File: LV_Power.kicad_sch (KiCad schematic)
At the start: 0 parts

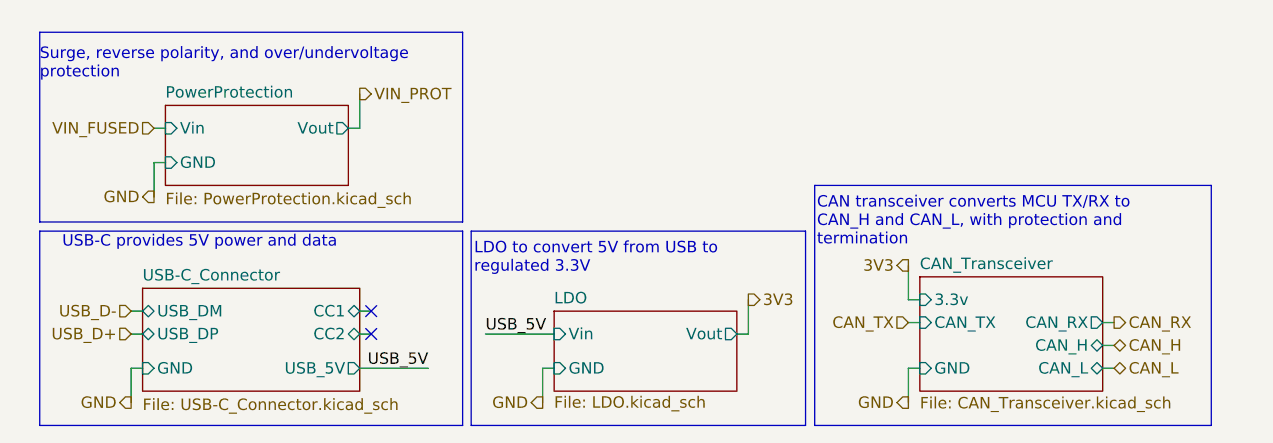
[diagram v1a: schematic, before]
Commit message: seperated hv+ and hv- for main and motor
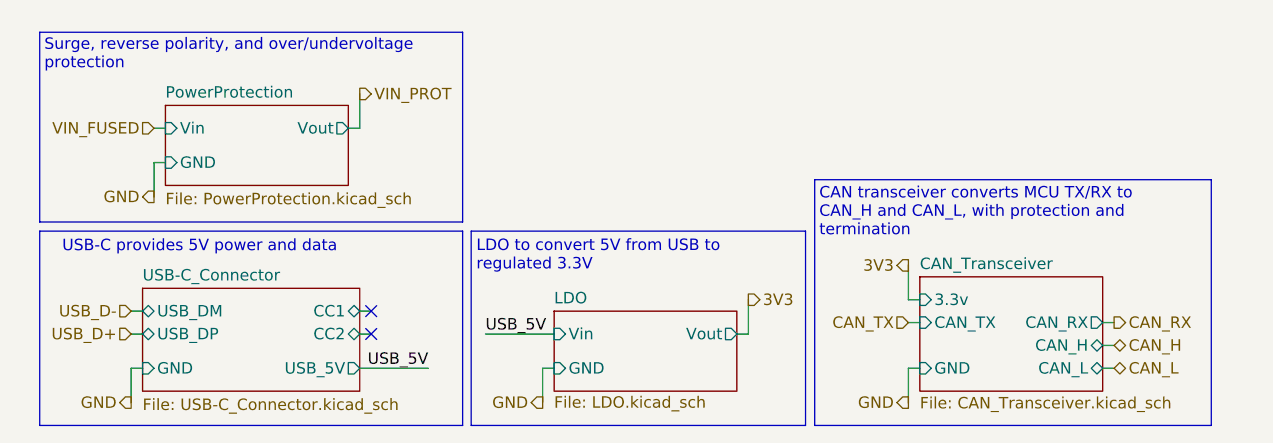
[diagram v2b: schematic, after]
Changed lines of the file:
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@@
 	(paper "A4")
 	(rectangle
-		(start 100.076 31.75)
+		(start 100.076 31.115)
 		(end 144.145 58.42)
 		(stroke
@@
 	(text "LDO to convert 5V from USB to \nregulated 3.3V"
 		(exclude_from_sim no)
-		(at 62.23 38.1 0)
+		(at 62.484 37.846 0)
 		(effects
 			(font
@@
 	(text "Surge, reverse polarity, and over/undervoltage \nprotection"
 		(exclude_from_sim no)
-		(at 13.97 16.51 0)
+		(at 14.478 15.494 0)
 		(effects
 			(font
@@
 	(text "USB-C provides 5V power and data"
 		(exclude_from_sim no)
-		(at 31.75 38.1 0)
+		(at 31.75 38.608 0)
 		(effects
 			(font
@@
 	(text "CAN transceiver converts MCU TX/RX to \nCAN_H and CAN_L, with protection and \ntermination"
 		(exclude_from_sim no)
-		(at 100.33 33.02 0)
+		(at 100.584 32.004 0)
 		(effects
 			(font

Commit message: dnp 0 ohm resistor across power protection
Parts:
- added R?: 0, symbol Device:R
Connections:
- net VIN_FUSED: now also R?.1
- net VIN_PROT: now also R?.2
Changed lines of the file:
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@@
 		)
+	)
+	(junction
+		(at 48.26 25.4)
+		(diameter 0)
+		(color 0 0 0 0)
+	)
+	(junction
+		(at 27.94 25.4)
+		(diameter 0)
+		(color 0 0 0 0)
 	)
 	(no_connect
@@
 	(wire
 		(pts
+			(xy 27.94 26.67) (xy 27.94 25.4)
+		)
+		(stroke
+			(width 0)
+			(type default)
+		)
+	)
+	(wire
+		(pts
 			(xy 110.49 46.99) (xy 111.76 46.99)
 		)
@@
 	(wire
 		(pts
+			(xy 27.94 26.67) (xy 34.29 26.67)
+		)
+		(stroke
+			(width 0)
+			(type default)
+		)
+	)
+	(wire
+		(pts
 			(xy 92.71 48.26) (xy 91.44 48.26)
 		)
@@
 	(wire
 		(pts
+			(xy 41.91 26.67) (xy 48.26 26.67)
+		)
+		(stroke
+			(width 0)
+			(type default)
+		)
+	)
+	(wire
+		(pts
 			(xy 110.49 52.07) (xy 111.76 52.07)
 		)
@@
 		(pts
 			(xy 110.49 44.45) (xy 110.49 40.64)
+		)
+		(stroke
+			(width 0)
+			(type default)
+		)
+	)
+	(wire
+		(pts
+			(xy 48.26 26.67) (xy 48.26 25.4)
 		)
 		(stroke
@@
 		)
 	)
+	(symbol
+		(lib_id "Device:R")
+		(at 38.1 26.67 90)
+		(unit 1)
+		(body_style 1)
+		(exclude_from_sim no)
+		(in_bom yes)
+		(on_board yes)
+		(in_pos_files yes)
+		(dnp yes)
+		(property "Reference" "R?"
+			(at 38.1 24.638 90)
+			(show_name no)
+			(do_not_autoplace no)
+			(effects
+				(font
+					(size 1.27 1.27)
+				)
+			)
+		)
+		(property "Value" "0"
+			(at 38.1 28.956 90)
+			(show_name no)
+			(do_not_autoplace no)
+			(effects
+				(font
+					(size 1.27 1.27)
+				)
+			)
+		)
+		(property "Footprint" ""
+			(at 38.1 28.448 90)
+			(hide yes)
+			(show_name no)
+			(do_not_autoplace no)
+			(effects
+				(font
+					(size 1.27 1.27)
+				)
+			)
+		)
+		(property "Datasheet" ""
+			(at 38.1 26.67 0)
+			(hide yes)
+			(show_name no)
+			(do_not_autoplace no)
+			(effects
+				(font
+					(size 1.27 1.27)
+				)
+			)
+		)
+		(property "Description" "Resistor"
+			(at 38.1 26.67 0)
+			(hide yes)
+			(show_name no)
+			(do_not_autoplace no)
+			(effects
+				(font
+					(size 1.27 1.27)
+				)
+			)
+		)
+		(pin "2"
+		)
+		(pin "1"
+		)
+		(instances
+			(project "PS-PrechargeBoard"
+				(path "/74d17fe6-68d4-4bd7-954a-e2bbb58b1f1e/2ca150cf-fbe5-4d5b-a7dc-f2dc5c6024d0"
+					(reference "R?")
+					(unit 1)
+				)
+			)
+		)
+	)

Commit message: AGND
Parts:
- gave numbers to parts that had none: 1
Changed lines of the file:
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@@
 	(text "LDO to convert 5V from USB to \nregulated 3.3V"
 		(exclude_from_sim no)
-		(at 62.484 37.846 0)
+		(at 62.23 38.1 0)
 		(effects
 			(font
@@
 	(text "Surge, reverse polarity, and over/undervoltage \nprotection"
 		(exclude_from_sim no)
-		(at 14.478 15.494 0)
+		(at 13.97 15.24 0)
 		(effects
 			(font
@@
 	(text "USB-C provides 5V power and data"
 		(exclude_from_sim no)
-		(at 31.75 38.608 0)
+		(at 31.75 38.1 0)
 		(effects
 			(font
@@
 	(text "CAN transceiver converts MCU TX/RX to \nCAN_H and CAN_L, with protection and \ntermination"
 		(exclude_from_sim no)
-		(at 100.584 32.004 0)
+		(at 100.33 31.75 0)
 		(effects
 			(font
@@
 	)
 	(hierarchical_label "GND"
-		(shape output)
+		(shape bidirectional)
 		(at 69.85 55.88 180)
 		(effects
@@
 	)
 	(hierarchical_label "GND"
-		(shape output)
+		(shape bidirectional)
 		(at 24.13 55.88 180)
 		(effects
@@
 	)
 	(hierarchical_label "GND"
-		(shape output)
+		(shape bidirectional)
 		(at 26.67 33.02 180)
 		(effects
@@
 	)
 	(hierarchical_label "GND"
-		(shape output)
+		(shape bidirectional)
 		(at 110.49 55.88 180)
 		(effects
@@
 		(in_pos_files yes)
 		(dnp yes)
-		(property "Reference" "R?"
+		(property "Reference" "R56"
 			(at 38.1 24.638 90)
 			(show_name no)
@@
 			(project "PS-PrechargeBoard"
 				(path "/74d17fe6-68d4-4bd7-954a-e2bbb58b1f1e/2ca150cf-fbe5-4d5b-a7dc-f2dc5c6024d0"
-					(reference "R?")
+					(reference "R56")
 					(unit 1)
 				)

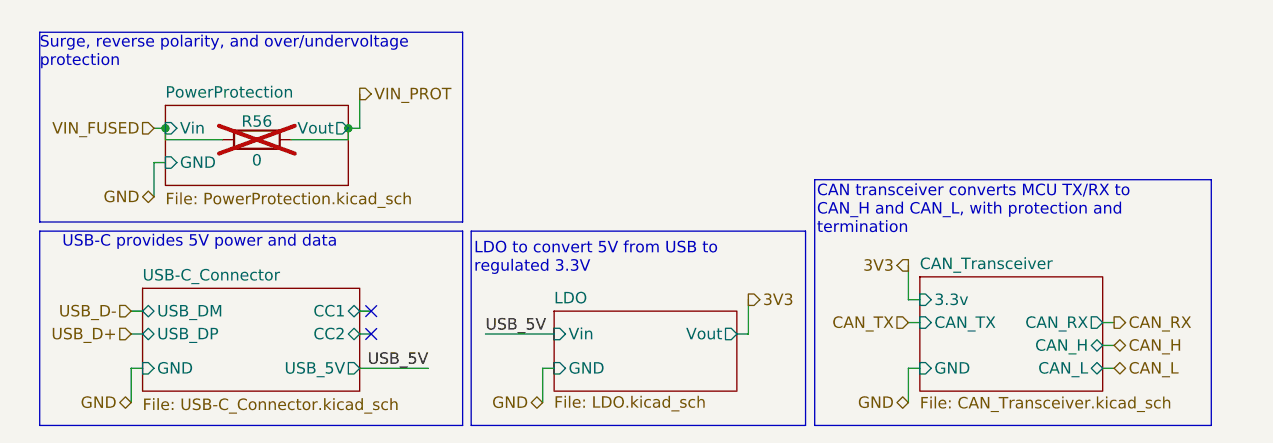
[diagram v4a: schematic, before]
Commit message: rx/tx fixed on can_transceiver
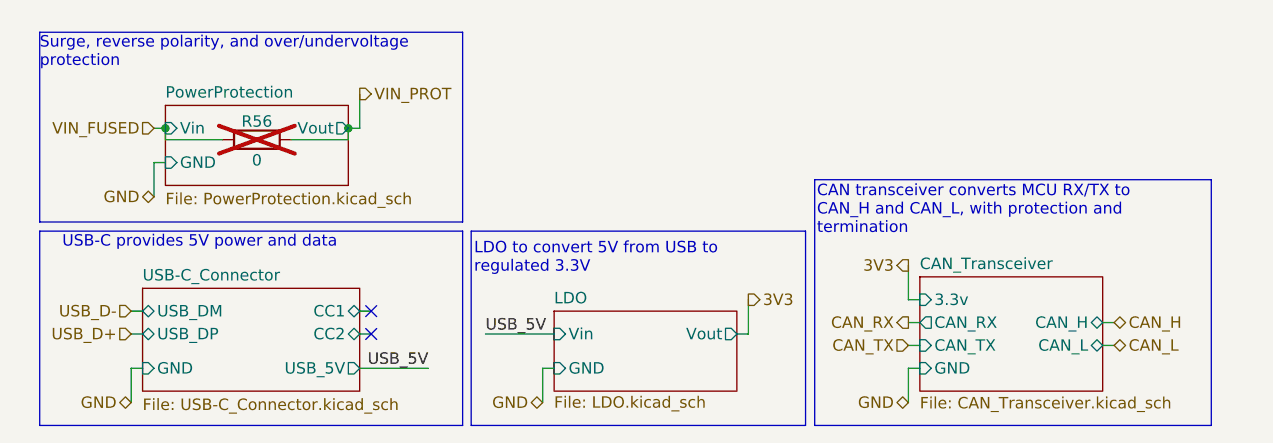
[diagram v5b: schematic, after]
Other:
- note added: "CAN transceiver converts MCU RX/TX to CAN_H and CAN_L, with protection and termination"
- note removed: "CAN transceiver converts MCU TX/RX to CAN_H and CAN_L, with protection and termination"
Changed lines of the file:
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@@
 		)
 	)
-	(text "CAN transceiver converts MCU TX/RX to \nCAN_H and CAN_L, with protection and \ntermination"
+	(text "CAN transceiver converts MCU RX/TX to \nCAN_H and CAN_L, with protection and \ntermination"
 		(exclude_from_sim no)
 		(at 100.33 31.75 0)
@@
 	(wire
 		(pts
+			(xy 110.49 49.53) (xy 111.76 49.53)
+		)
+		(stroke
+			(width 0)
+			(type default)
+		)
+	)
+	(wire
+		(pts
+			(xy 26.67 25.4) (xy 27.94 25.4)
+		)
+		(stroke
+			(width 0)
+			(type default)
+		)
+	)
+	(wire
+		(pts
+			(xy 24.13 45.72) (xy 25.4 45.72)
+		)
+		(stroke
+			(width 0)
+			(type default)
+		)
+	)
+	(wire
+		(pts
+			(xy 132.08 46.99) (xy 133.35 46.99)
+		)
+		(stroke
+			(width 0)
+			(type default)
+		)
+	)
+	(wire
+		(pts
 			(xy 110.49 46.99) (xy 111.76 46.99)
 		)
@@
 	(wire
 		(pts
-			(xy 26.67 25.4) (xy 27.94 25.4)
-		)
-		(stroke
-			(width 0)
-			(type default)
-		)
-	)
-	(wire
-		(pts
-			(xy 24.13 45.72) (xy 25.4 45.72)
+			(xy 49.53 25.4) (xy 48.26 25.4)
+		)
+		(stroke
+			(width 0)
+			(type default)
+		)
+	)
+	(wire
+		(pts
+			(xy 49.53 48.26) (xy 50.8 48.26)
+		)
+		(stroke
+			(width 0)
+			(type default)
+		)
+	)
+	(wire
+		(pts
+			(xy 49.53 45.72) (xy 50.8 45.72)
+		)
+		(stroke
+			(width 0)
+			(type default)
+		)
+	)
+	(wire
+		(pts
+			(xy 24.13 48.26) (xy 25.4 48.26)
+		)
+		(stroke
+			(width 0)
+			(type default)
+		)
+	)
+	(wire
+		(pts
+			(xy 24.13 55.88) (xy 24.13 52.07)
+		)
+		(stroke
+			(width 0)
+			(type default)
+		)
+	)
+	(wire
+		(pts
+			(xy 110.49 44.45) (xy 111.76 44.45)
+		)
+		(stroke
+			(width 0)
+			(type default)
+		)
+	)
+	(wire
+		(pts
+			(xy 69.85 52.07) (xy 71.12 52.07)
+		)
+		(stroke
+			(width 0)
+			(type default)
+		)
+	)
+	(wire
+		(pts
+			(xy 27.94 26.67) (xy 34.29 26.67)
+		)
+		(stroke
+			(width 0)
+			(type default)
+		)
+	)
+	(wire
+		(pts
+			(xy 92.71 48.26) (xy 91.44 48.26)
+		)
+		(stroke
+			(width 0)
+			(type default)
+		)
+	)
+	(wire
+		(pts
+			(xy 92.71 48.26) (xy 92.71 44.45)
+		)
+		(stroke
+			(width 0)
+			(type default)
+		)
+	)
+	(wire
+		(pts
+			(xy 26.67 29.21) (xy 27.94 29.21)
+		)
+		(stroke
+			(width 0)
+			(type default)
+		)
+	)
+	(wire
+		(pts
+			(xy 69.85 55.88) (xy 69.85 52.07)
+		)
+		(stroke
+			(width 0)
+			(type default)
+		)
+	)
+	(wire
+		(pts
+			(xy 26.67 33.02) (xy 26.67 29.21)
+		)
+		(stroke
+			(width 0)
+			(type default)
+		)
+	)
+	(wire
+		(pts
+			(xy 24.13 52.07) (xy 25.4 52.07)
+		)
+		(stroke
+			(width 0)
+			(type default)
+		)
+	)
+	(wire
+		(pts
+			(xy 110.49 55.88) (xy 110.49 52.07)
+		)
+		(stroke
+			(width 0)
+			(type default)
+		)
+	)
+	(wire
+		(pts
+			(xy 63.5 48.26) (xy 71.12 48.26)
+		)
+		(stroke
+			(width 0)
+			(type default)
+		)
+	)
+	(wire
+		(pts
+			(xy 49.53 21.59) (xy 49.53 25.4)
 		)
 		(stroke
@@
 		(pts
 			(xy 133.35 49.53) (xy 132.08 49.53)
-		)
-		(stroke
-			(width 0)
-			(type default)
-		)
-	)
-	(wire
-		(pts
-			(xy 49.53 25.4) (xy 48.26 25.4)
-		)
-		(stroke
-			(width 0)
-			(type default)
-		)
-	)
-	(wire
-		(pts
-			(xy 49.53 48.26) (xy 50.8 48.26)
-		)
-		(stroke
-			(width 0)
-			(type default)
-		)
-	)
-	(wire
-		(pts
-			(xy 133.35 46.99) (xy 132.08 46.99)
-		)
-		(stroke
-			(width 0)
-			(type default)
-		)
-	)
-	(wire
-		(pts
-			(xy 49.53 45.72) (xy 50.8 45.72)
-		)
-		(stroke
-			(width 0)
-			(type default)
-		)
-	)
-	(wire
-		(pts
-			(xy 24.13 48.26) (xy 25.4 48.26)
-		)
-		(stroke
-			(width 0)
-			(type default)
-		)
-	)
-	(wire
-		(pts
-			(xy 24.13 55.88) (xy 24.13 52.07)
-		)
-		(stroke
-			(width 0)
-			(type default)
-		)
-	)
-	(wire
-		(pts
-			(xy 110.49 44.45) (xy 111.76 44.45)
-		)
-		(stroke
-			(width 0)
-			(type default)
-		)
-	)
-	(wire
-		(pts
-			(xy 69.85 52.07) (xy 71.12 52.07)
-		)
-		(stroke
-			(width 0)
-			(type default)
-		)
-	)
-	(wire
-		(pts
-			(xy 27.94 26.67) (xy 34.29 26.67)
-		)
-		(stroke
-			(width 0)
-			(type default)
-		)
-	)
-	(wire
-		(pts
-			(xy 92.71 48.26) (xy 91.44 48.26)
-		)
-		(stroke
-			(width 0)
-			(type default)
-		)
-	)
-	(wire
-		(pts
-			(xy 92.71 48.26) (xy 92.71 44.45)
-		)
-		(stroke
-			(width 0)
-			(type default)
-		)
-	)
-	(wire
-		(pts
-			(xy 26.67 29.21) (xy 27.94 29.21)
-		)
-		(stroke
-			(width 0)
-			(type default)
-		)
-	)
-	(wire
-		(pts
-			(xy 69.85 55.88) (xy 69.85 52.07)
-		)
-		(stroke
-			(width 0)
-			(type default)
-		)
-	)
-	(wire
-		(pts
-			(xy 26.67 33.02) (xy 26.67 29.21)
-		)
-		(stroke
-			(width 0)
-			(type default)
-		)
-	)
-	(wire
-		(pts
-			(xy 24.13 52.07) (xy 25.4 52.07)
-		)
-		(stroke
-			(width 0)
-			(type default)
-		)
-	)
-	(wire
-		(pts
-			(xy 110.49 55.88) (xy 110.49 52.07)
-		)
-		(stroke
-			(width 0)
-			(type default)
-		)
-	)
-	(wire
-		(pts
-			(xy 63.5 48.26) (xy 71.12 48.26)
-		)
-		(stroke
-			(width 0)
-			(type default)
-		)
-	)
-	(wire
-		(pts
-			(xy 49.53 21.59) (xy 49.53 25.4)
-		)
-		(stroke
-			(width 0)
-			(type default)
-		)
-	)
-	(wire
-		(pts
-			(xy 133.35 52.07) (xy 132.08 52.07)
 		)
 		(stroke
@@
 	(hierarchical_label "CAN_TX"
 		(shape input)
-		(at 110.49 46.99 180)
+		(at 110.49 49.53 180)
 		(effects
 			(font
@@
 	(hierarchical_label "CAN_L"
 		(shape bidirectional)
-		(at 133.35 52.07 0)
+		(at 133.35 49.53 0)
 		(effects
 			(font
@@
 	(hierarchical_label "CAN_RX"
 		(shape output)
-		(at 133.35 46.99 0)
-		(effects
-			(font
-				(size 1.27 1.27)
-			)
-			(justify left)
+		(at 110.49 46.99 180)
+		(effects
+			(font
+				(size 1.27 1.27)
+			)
+			(justify right)
 		)
 	)
@@
 	(hierarchical_label "CAN_H"
 		(shape bidirectional)
-		(at 133.35 49.53 0)
+		(at 133.35 46.99 0)
 		(effects
 			(font
@@
 		)
 		(pin "CAN_H" bidirectional
+			(at 132.08 46.99 0)
+			(effects
+				(font
+					(size 1.27 1.27)
+				)
+				(justify right)
+			)
+		)
+		(pin "CAN_L" bidirectional
 			(at 132.08 49.53 0)
 			(effects
@@
 			)
 		)
-		(pin "CAN_L" bidirectional
-			(at 132.08 52.07 0)
-			(effects
-				(font
-					(size 1.27 1.27)
-				)
-				(justify right)
-			)
-		)
 		(pin "CAN_RX" output
-			(at 132.08 46.99 0)
-			(effects
-				(font
-					(size 1.27 1.27)
-				)
-				(justify right)
+			(at 111.76 46.99 180)
+			(effects
+				(font
+					(size 1.27 1.27)
+				)
+				(justify left)
 			)
 		)
 		(pin "CAN_TX" input
-			(at 111.76 46.99 180)
-			(effects
-				(font
+			(at 111.76 49.53 180)
+			(effects
+				(font

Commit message: made lv hierarchical input pin cute
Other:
- note added: "CAN transceiver converts MCU TX/RX to CAN_H and CAN_L, with protection and termination"
- note removed: "CAN transceiver converts MCU RX/TX to CAN_H and CAN_L, with protection and termination"
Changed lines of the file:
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@@
 		)
 	)
-	(text "CAN transceiver converts MCU RX/TX to \nCAN_H and CAN_L, with protection and \ntermination"
+	(text "CAN transceiver converts MCU TX/RX to \nCAN_H and CAN_L, with protection and \ntermination"
 		(exclude_from_sim no)
 		(at 100.33 31.75 0)
@@
 	(wire
 		(pts
+			(xy 110.49 46.99) (xy 111.76 46.99)
+		)
+		(stroke
+			(width 0)
+			(type default)
+		)
+	)
+	(wire
+		(pts
+			(xy 26.67 25.4) (xy 27.94 25.4)
+		)
+		(stroke
+			(width 0)
+			(type default)
+		)
+	)
+	(wire
+		(pts
+			(xy 24.13 45.72) (xy 25.4 45.72)
+		)
+		(stroke
+			(width 0)
+			(type default)
+		)
+	)
+	(wire
+		(pts
+			(xy 132.08 46.99) (xy 133.35 46.99)
+		)
+		(stroke
+			(width 0)
+			(type default)
+		)
+	)
+	(wire
+		(pts
 			(xy 110.49 49.53) (xy 111.76 49.53)
-		)
-		(stroke
-			(width 0)
-			(type default)
-		)
-	)
-	(wire
-		(pts
-			(xy 26.67 25.4) (xy 27.94 25.4)
-		)
-		(stroke
-			(width 0)
-			(type default)
-		)
-	)
-	(wire
-		(pts
-			(xy 24.13 45.72) (xy 25.4 45.72)
-		)
-		(stroke
-			(width 0)
-			(type default)
-		)
-	)
-	(wire
-		(pts
-			(xy 132.08 46.99) (xy 133.35 46.99)
-		)
-		(stroke
-			(width 0)
-			(type default)
-		)
-	)
-	(wire
-		(pts
-			(xy 110.49 46.99) (xy 111.76 46.99)
 		)
 		(stroke
@@
 	(hierarchical_label "CAN_TX"
 		(shape input)
-		(at 110.49 49.53 180)
+		(at 110.49 46.99 180)
 		(effects
 			(font
@@
 	(hierarchical_label "CAN_RX"
 		(shape output)
-		(at 110.49 46.99 180)
+		(at 110.49 49.53 180)
 		(effects
 			(font
@@
 		)
 		(pin "CAN_RX" output
+			(at 111.76 49.53 180)
+			(effects
+				(font
+					(size 1.27 1.27)
+				)
+				(justify left)
+			)
+		)
+		(pin "CAN_TX" input
 			(at 111.76 46.99 180)
 			(effects
 				(font
-					(size 1.27 1.27)
-				)
-				(justify left)
-			)
-		)
-		(pin "CAN_TX" input
-			(at 111.76 49.53 180)
-			(effects
-				(font

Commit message: voltage sensor cleanup
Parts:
- renumbered R56 to R57
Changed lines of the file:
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@@
 		(in_pos_files yes)
 		(dnp yes)
-		(property "Reference" "R56"
+		(property "Reference" "R57"
 			(at 38.1 24.638 90)
 			(show_name no)
@@
 			(project "PS-PrechargeBoard"
 				(path "/74d17fe6-68d4-4bd7-954a-e2bbb58b1f1e/2ca150cf-fbe5-4d5b-a7dc-f2dc5c6024d0"
-					(reference "R56")
+					(reference "R57")
 					(unit 1)
 				)
@@
 			(project "PS-PrechargeBoard"
 				(path "/74d17fe6-68d4-4bd7-954a-e2bbb58b1f1e/2ca150cf-fbe5-4d5b-a7dc-f2dc5c6024d0"
-					(page "9")
+					(page "16")
 				)
 			)
@@
 			(project "PS-PrechargeBoard"
 				(path "/74d17fe6-68d4-4bd7-954a-e2bbb58b1f1e/2ca150cf-fbe5-4d5b-a7dc-f2dc5c6024d0"
-					(page "13")
+					(page "14")
 				)
 			)
@@
 			(project "PS-PrechargeBoard"
 				(path "/74d17fe6-68d4-4bd7-954a-e2bbb58b1f1e/2ca150cf-fbe5-4d5b-a7dc-f2dc5c6024d0"
-					(page "10")
+					(page "15")
 				)
 			)
@@
 			(project "PS-PrechargeBoard"
 				(path "/74d17fe6-68d4-4bd7-954a-e2bbb58b1f1e/2ca150cf-fbe5-4d5b-a7dc-f2dc5c6024d0"
-					(page "11")
-				)
-			)
+					(page "13")
+				)
+			)

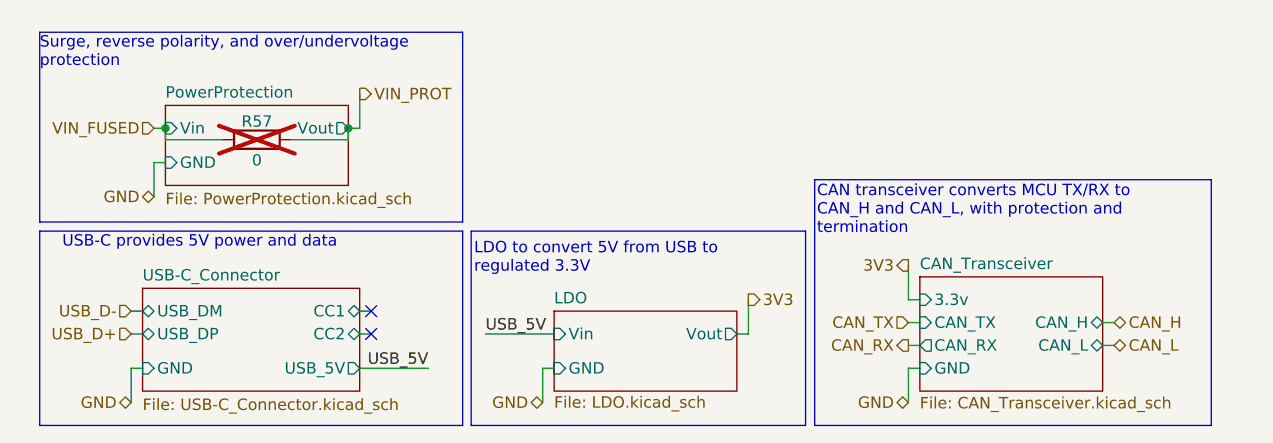
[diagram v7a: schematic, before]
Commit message: updated usb-c connector
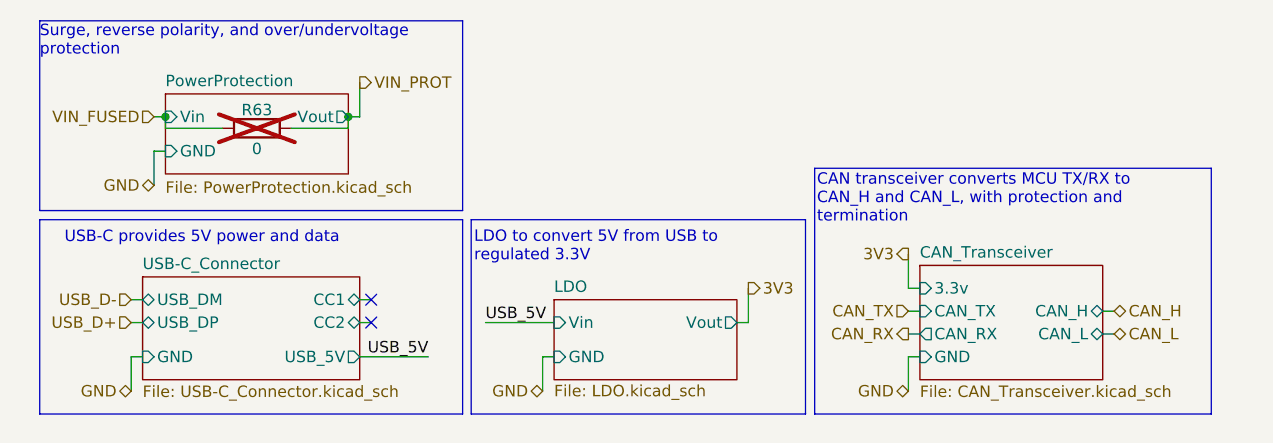
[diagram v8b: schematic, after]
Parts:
- renumbered R57 to R63
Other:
- moved on the sheet: R63
